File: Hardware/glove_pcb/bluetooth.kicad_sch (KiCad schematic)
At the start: 12 parts, among them J3 Conn_01x01, U10 74LVC1T45GW_125, U8 74LVC1T45GW_125, U9 BM70BLES1FC2-0002AA

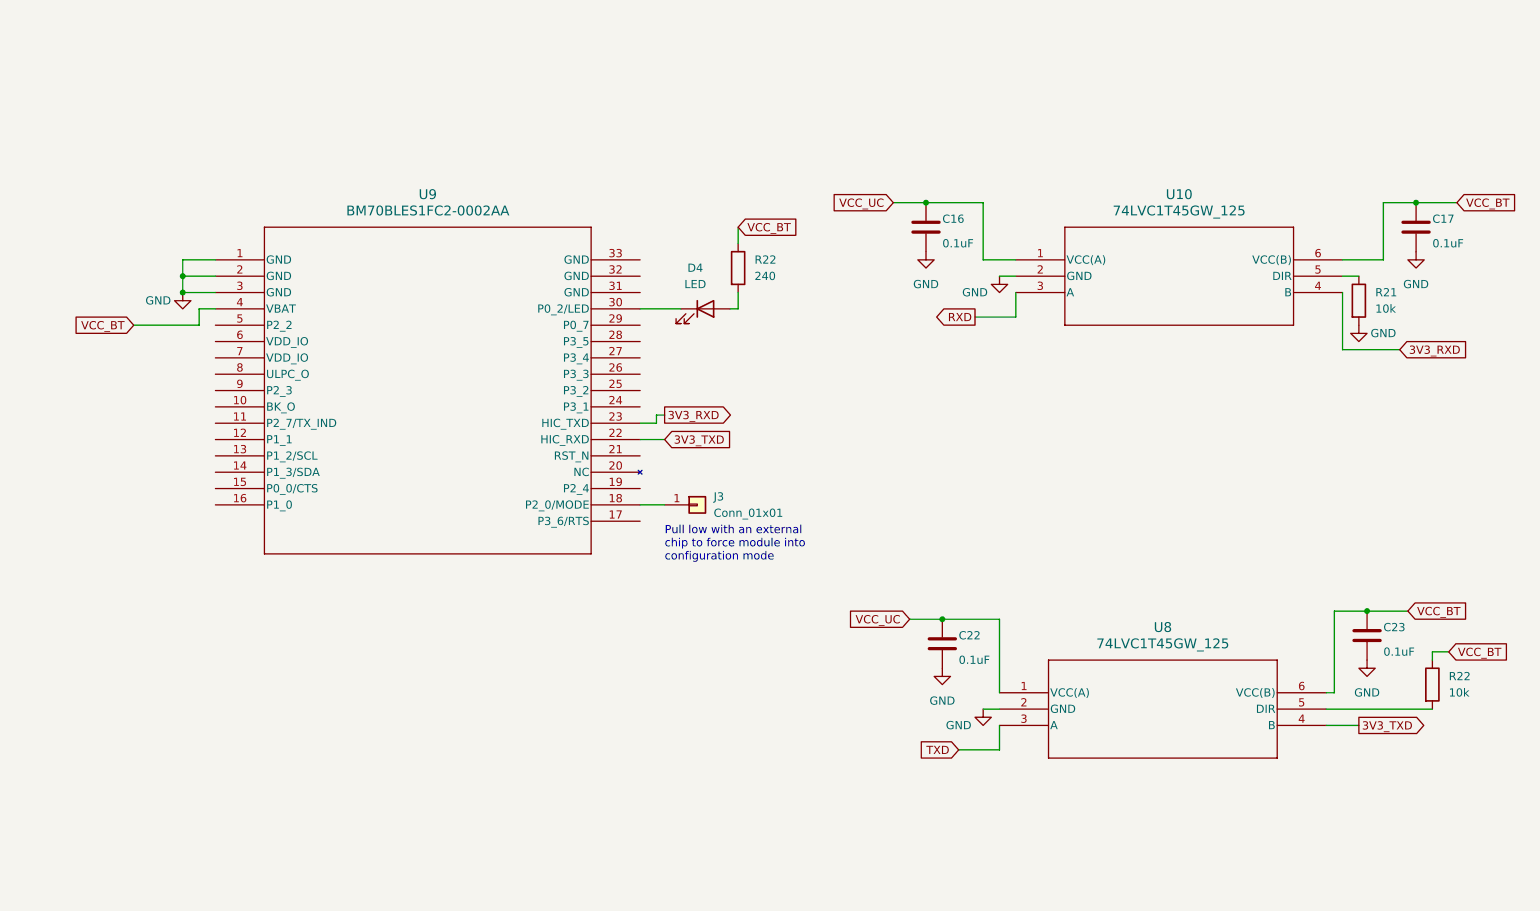
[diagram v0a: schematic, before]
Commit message: Add titles to pages and reannotate
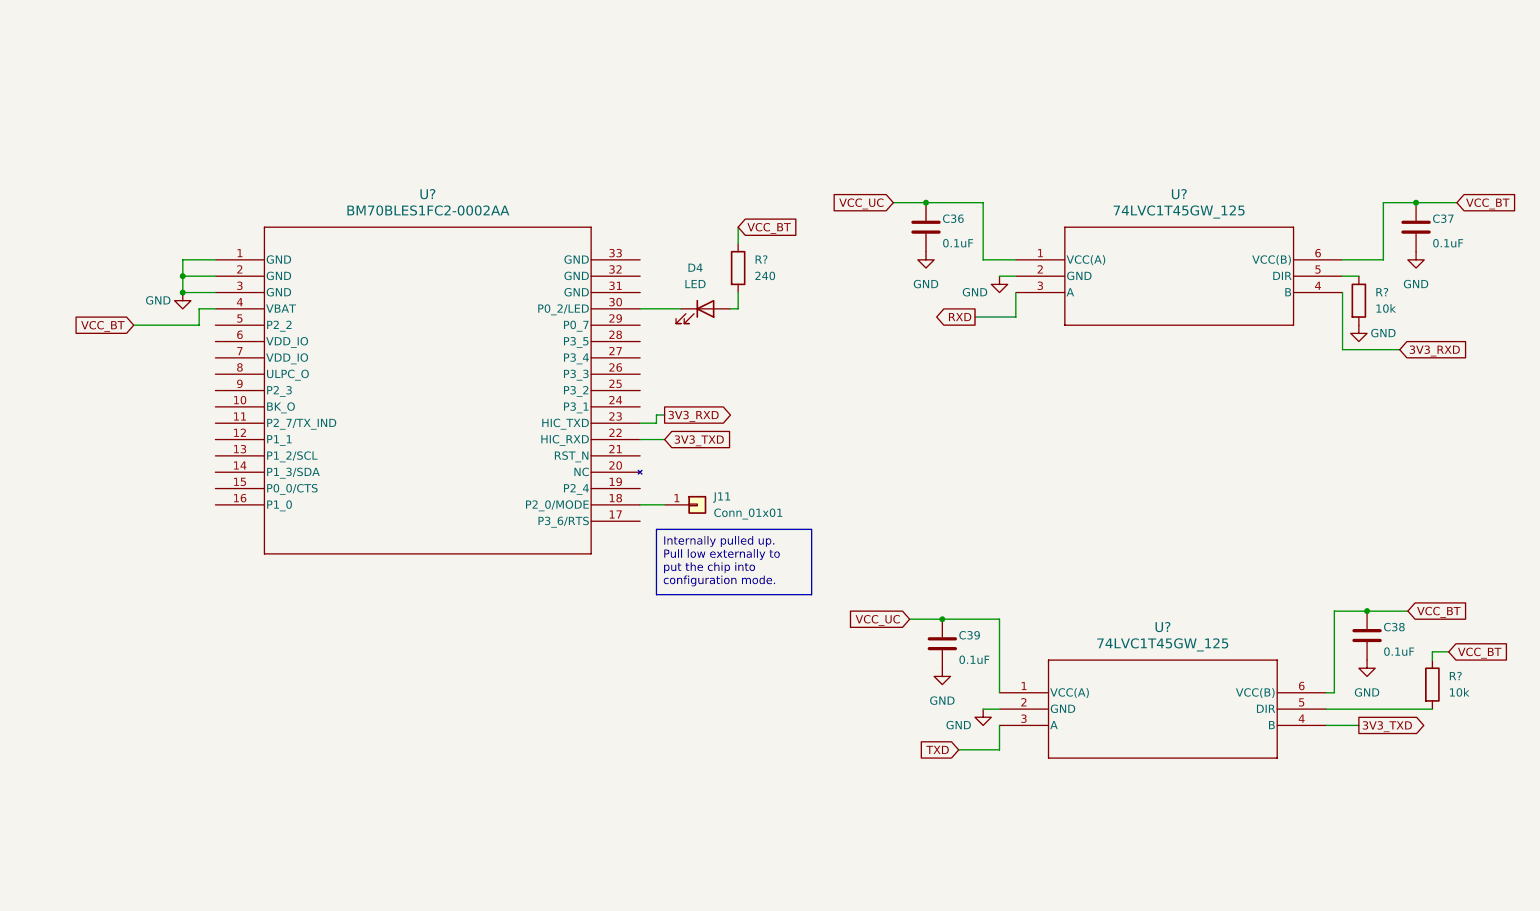
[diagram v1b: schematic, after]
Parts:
- renumbered C16 to C36, C17 to C37, C23 to C38, C22 to C39, J3 to J11, R21 to R?, R22 to R?, U8 to U?, U9 to U?, U10 to U?
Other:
- note removed: "Pull low with an external chip to force module into configuration mode"
- company: (none) -> COEN 490 Team 15
- title: (none) -> Bluetooth Communication

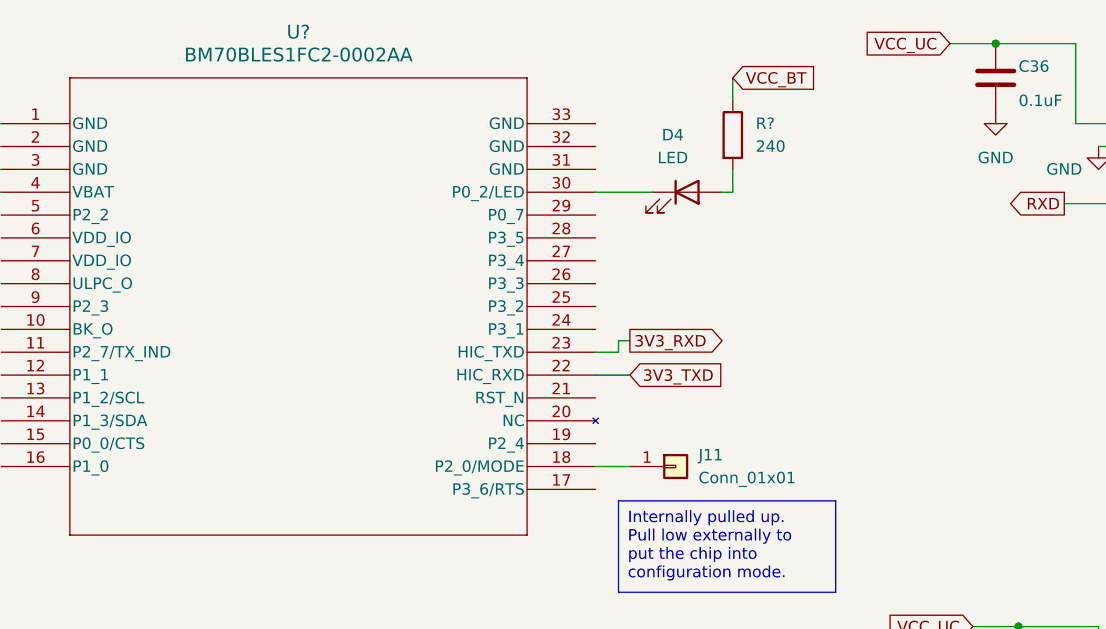
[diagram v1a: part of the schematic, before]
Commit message: Finalize schematic for real this time
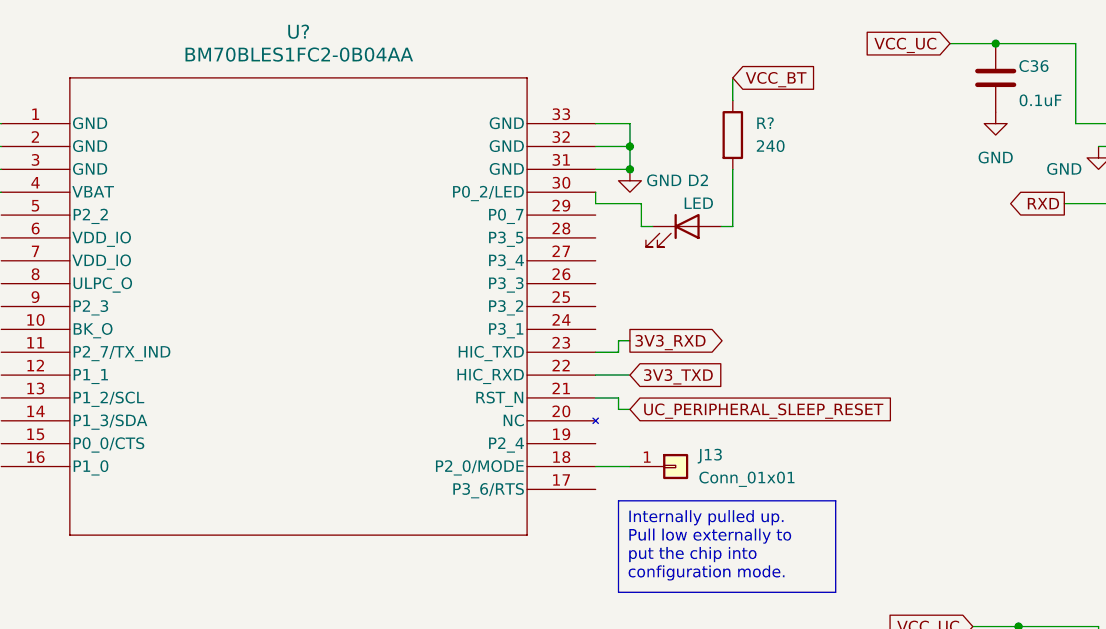
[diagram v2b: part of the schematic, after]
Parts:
- U?: value BM70BLES1FC2-0002AA -> BM70BLES1FC2-0B04AA; symbol Glove_Symbols:BM70BLES1FC2-0002AA -> Glove_Symbols:BM70BLES1FC2-0B04AA
- renumbered D4 to D2, J11 to J13
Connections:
- net GND: now also U?.31 (GND), U?.32 (GND), U?.33 (GND)
- net UC_PERIPHERAL_SLEEP_RESET: now reaches U?.21 (RST_N)
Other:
- moved on the sheet: D2
